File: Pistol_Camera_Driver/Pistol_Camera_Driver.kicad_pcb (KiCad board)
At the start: 2 copper layers, 95.8 x 46.1 mm, 102 parts, among them J1 Screw_Terminal_01x02, J10 Bluetooth, J11 Screw_Terminal_01x02, J12 Screw_Terminal_01x02, J13 I2C, J14 Screw_Terminal_01x02, J15 Screw_Terminal_01x02, J2 Objective, J3 Screw_Terminal_01x02, J4 Screw_Terminal_01x02, J5 Screw_Terminal_01x02, J6 Joystick, J7 Screw_Terminal_01x02, J8 Screw_Terminal_01x02, J9 Screw_Terminal_01x02, K1 IM03, Q1 locked, U1 LM7805_TO220, U2 LM317_TO-263, U3 Raspberri_Pi_Pico, U4 DRV8834PWP, U5 DRV8834PWP

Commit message: V0.2 Seems 2B ready
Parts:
- removed C23: 2u2, Capacitor_SMD:C_0603_1608Metric_Pad1.08x0.95mm_HandSolder
- removed the REF** at (73.6, 74.7)
- removed the REF** at (73.6, 35.6)
- removed the REF** at (27.6, 74.7)
- removed U2: LM317_TO-263, Package_TO_SOT_SMD:TO-263-2
- removed U3: Raspberri_Pi_Pico, Shield_Emergent:Raspberry Pi Pico
- added D2: CDBA3100-HF, Diode_SMD:D_SMA, F.Cu at (96.8, 58.8)
- added J16: Screw_Terminal_01x02, Connector_PinSocket_2.54mm:PinSocket_1x02_P2.54mm_Vertical, F.Cu at (48.3, 62.0)
- added J17: Screw_Terminal_01x02, Connector_PinSocket_2.54mm:PinSocket_1x02_P2.54mm_Vertical, F.Cu at (47.3, 58.4)
- added L5: 22u, Inductor_SMD:L_Sunlord_SWPA4012S, F.Cu at (102.4, 68.1)
- added U10: ~, Vedro:RP2040Zero, F.Cu at (58.1, 47.6)
- C10, C12, C5, C7, C8, R1, R10, R11, R12, R14, R15, R16, R18, R2, R4, R5, R7, R8, R9: moved to F.Cu
- C13, C15, C16, C17, C19, C20, C22: value 2u2 -> 22u
- C2: value 0.33 -> 0.1; moved to F.Cu
- C3: value 0.1 -> 22u; moved to F.Cu
- C4: value 1 -> 470uF; footprint Capacitor_SMD:C_0603_1608Metric_Pad1.08x0.95mm_HandSolder -> Capacitor_THT:CP_Radial_D6.3mm_P2.50mm; moved to F.Cu
- C6: value 1 -> 180uF; footprint Capacitor_SMD:C_0603_1608Metric_Pad1.08x0.95mm_HandSolder -> Capacitor_THT:CP_Radial_D6.3mm_P2.50mm; moved to F.Cu
- J2: moved to B.Cu
- L1, L2, L3, L4: value L -> 4u7; footprint Inductor_SMD:L_12x12mm_H8mm -> Inductor_SMD:L_Chilisin_BMRx00040412
- R3: value 240 -> 4k7; moved to F.Cu
- R6: value 390 -> 4k7; moved to F.Cu
- U1: value LM7805_TO220 -> XL1509-3.3; footprint Package_TO_SOT_THT:TO-220-3_Vertical -> Package_SO:SOIC-8-1EP_3.9x4.9mm_P1.27mm_EP2.95x4.9mm_Mask2.71x3.4mm_ThermalVias
- U4, U5: footprint Shield_Emergent:DRV8834PWP -> Vedro:DRV8834PWP; moved to F.Cu
- locked: renamed from C11; moved to F.Cu
- moved R36 101.4 mm to (79.1, 68.5), turned to 90 degrees
- moved C22 101.4 mm to (73.9, 74.0), turned to 90 degrees
- moved R35 100.9 mm to (80.7, 68.5), turned to 90 degrees
- moved R39 100.6 mm to (77.5, 68.5), turned to 90 degrees
- moved R38 99.4 mm to (76.6, 57.3), turned to 90 degrees
- moved R31 92.6 mm to (78.2, 57.3), turned to 90 degrees
- moved R30 91.5 mm to (79.8, 57.3), turned to 90 degrees
- moved R29 90.4 mm to (81.4, 57.3), turned to 90 degrees
- moved C19 89.6 mm to (73.1, 62.6), turned to 90 degrees
- moved R28 89.4 mm to (83.0, 57.3), turned to 90 degrees
- moved R34 89.3 mm to (82.3, 68.5), turned to 90 degrees
- moved R37 88.9 mm to (85.8, 45.5), turned to 90 degrees
- moved R27 88.5 mm to (84.6, 57.3), turned to 90 degrees
- moved C24 88.5 mm to (84.6, 71.6), turned to 180 degrees
- moved R33 88.2 mm to (83.9, 68.5), turned to 90 degrees
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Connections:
- C14 pad 2: +12V -> +5V
- C15 pad 1: +12V -> +5V
- C16 pad 1: +12V -> +5V
- C18 pad 2: +12V -> +5V
- C19 pad 1: +12V -> +5V
- C2 pad 1: +12V -> +5V
- C20 pad 1: Net-(J9-Pin_1) -> Net-(J12-Pin_1)
- C21 pad 2: +12V -> +5V
- C22 pad 1: +12V -> +5V
- C24 pad 2: +12V -> +5V
- C3 pad 1: +5V -> Net-(J9-Pin_1)
- C4 pad 1: +12V -> +5V
- J10 pad 3: GND -> +3V3
- J10 pad 4: +5V -> GND
- J13 pad 1: SDA -> SCL
- J13 pad 2: SCL -> SDA
- J13 pad 4: +5V -> +3V3
- J3 pad 1: +12V -> +5V
- J4 pad 1: +12V -> +5V
- R17 pad 1: Solenoid_DIR -> Solenoid_ON
- R19 pad 1: Solenoid_ON -> Solenoid_DIR
- R3 pad 1: +3.3VP -> +3V3
- R3 pad 2: Net-(U2-ADJ) -> SCL
- R6 pad 1: Net-(U2-ADJ) -> +3V3
- R6 pad 2: GND -> SDA
- U1 pad 1: +12V -> +5V
- U1 pad 2: GND -> Net-(U1-OUT)
- U1 pad 3: +5V -> +3.3VP
- U6 pad 3: +12V -> +5V
- U6 pad 4: PWM_UV -> PWM_WHITE
- U6 pad 8: +12V -> +5V
- U7 pad 3: +12V -> +5V
- U7 pad 4: PWM_WHITE -> PWM_RED
- U7 pad 8: +12V -> +5V
- U8 pad 3: +12V -> +5V
- U8 pad 4: PWM_RED -> PWM_UV
- U8 pad 8: +12V -> +5V
- U9 pad 3: +12V -> +5V
- U9 pad 8: +12V -> +5V
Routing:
- net +12V: track 115.9 -> 0.00 mm
- net +3V3: track 174.5 -> 116.5 mm, vias 5 -> 1
- net Solenoid_ON: track 3.29 -> 39.3 mm, vias 0 -> 2
- net MOTORS_nSLEEP: track 104.2 -> 71.9 mm, vias 3 -> 2
- net Solenoid_DIR: track 4.58 -> 36.0 mm, vias 0 -> 2
- net +3.3VP: track 114.8 -> 94.6 mm, vias 1 -> 0
- net PWM_WHITE: track 38.7 -> 23.0 mm
- net K3: track 9.70 -> 24.9 mm, vias 0 -> 2
- net K4: track 5.67 -> 20.2 mm, vias 0 -> 2
- net GND: track 30.1 -> 17.7 mm, vias 307 -> 213
- net (no net): track 11.9 -> 0.00 mm, vias 1 -> 0
- net nFLT2: track 56.2 -> 67.1 mm
- net STEP1: track 61.9 -> 51.2 mm
- net DIR1: track 60.1 -> 49.3 mm
- net nEN2: track 54.2 -> 43.8 mm
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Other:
- board size 95.8 x 46.1 mm -> 83.3 x 46.1 mm

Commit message: V0.3 Ordered
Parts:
- added REF**: MountingHole_3.2mm_M3, MountingHole:MountingHole_3.2mm_M3, F.Cu at (40.6, 74.7)
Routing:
- net GND: vias 213 -> 215
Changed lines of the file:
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@@
     (property "ki_keywords" "R res resistor")
     (attr smd)
-    (fp_text reference "R10" (at 0.25 2.25) (layer "F.SilkS")
+    (fp_text reference "R10" (at -3.6 0.65) (layer "F.SilkS")
         (effects (font (size 1 1) (thickness 0.15)))
     )
@@
     )
   )
+  (footprint "MountingHole:MountingHole_3.2mm_M3" locked (layer "F.Cu")
+    (at 40.645 74.65)
+    (descr "Mounting Hole 3.2mm, no annular, M3")
+    (tags "mounting hole 3.2mm no annular m3")
+    (attr exclude_from_pos_files exclude_from_bom)
+    (fp_text reference "REF**" (at 0 -4.2) (layer "F.SilkS") hide
+        (effects (font (size 1 1) (thickness 0.15)))
+    )
+    (fp_text value "MountingHole_3.2mm_M3" (at 0 4.2) (layer "F.Fab") hide
+        (effects (font (size 1 1) (thickness 0.15)))
+    )
+    (fp_text user "${REFERENCE}" (at 0 0) (layer "F.Fab") hide
+        (effects (font (size 1 1) (thickness 0.15)))
+    )
+    (fp_circle (center 0 0) (end 3.2 0)
+      (stroke (width 0.15) (type solid)) (fill none) (layer "Cmts.User"))
+    (fp_circle (center 0 0) (end 3.45 0)
+      (stroke (width 0.05) (type solid)) (fill none) (layer "F.CrtYd"))
+    (pad "" np_thru_hole circle locked (at 0 0) (size 3.2 3.2) (drill 3.2) (layers "F&B.Cu" "*.Mask"))
+  )
   (footprint "Capacitor_SMD:C_0603_1608Metric_Pad1.08x0.95mm_HandSolder" (layer "F.Cu")
     (at 112.65 41.85 180)
@@
     (property "ki_keywords" "diode Schottky")
     (attr smd)
-    (fp_text reference "D2" (at 0 -2.5 90) (layer "F.SilkS")
+    (fp_text reference "D2" (at -0.7 -2.5 90) (layer "F.SilkS")
         (effects (font (size 1 1) (thickness 0.15)))
     )
@@
         (effects (font (size 1 1) (thickness 0.15)) (justify mirror))
     )
-    (fp_text value "Objective" (at 2.875 -2.75) (layer "B.SilkS")
-        (effects (font (size 1 1) (thickness 0.15)) (justify mirror))
+    (fp_text value "Objective" (at -1.325 -2.9 180) (layer "F.SilkS")
+        (effects (font (size 1 1) (thickness 0.15)))
     )
     (fp_text user "${REFERENCE}" (at -2.525 -4.95) (layer "B.Fab")
@@
   (via (at 70.6 35.2) (size 0.9) (drill 0.4) (layers "F.Cu" "B.Cu") (free) (net 2))
   (via (at 75.25 49) (size 0.9) (drill 0.4) (layers "F.Cu" "B.Cu") (free) (net 2))
-  (via (at 84.628637 62.668266) (size 0.9) (drill 0.4) (layers "F.Cu" "B.Cu") (free) (net 2))
+  (via (at 85.65 61.9) (size 0.9) (drill 0.4) (layers "F.Cu" "B.Cu") (free) (net 2))
   (via (at 91 32.1) (size 0.9) (drill 0.4) (layers "F.Cu" "B.Cu") (free) (net 2))
   (via (at 38.9 40.5) (size 0.9) (drill 0.4) (layers "F.Cu" "B.Cu") (free) (net 2))
@@
   (via (at 118.55 63.95) (size 0.9) (drill 0.4) (layers "F.Cu" "B.Cu") (free) (net 2))
   (via (at 74.95 56.25) (size 0.9) (drill 0.4) (layers "F.Cu" "B.Cu") (free) (net 2))
+  (via (at 84.05 62.3) (size 0.9) (drill 0.4) (layers "F.Cu" "B.Cu") (free) (net 2))
   (via (at 38.65 46.75) (size 0.9) (drill 0.4) (layers "F.Cu" "B.Cu") (free) (net 2))
   (via (at 68.4 46.1) (size 0.9) (drill 0.4) (layers "F.Cu" "B.Cu") (free) (net 2))
@@
   (via (at 61.781858 41.884493) (size 0.9) (drill 0.4) (layers "F.Cu" "B.Cu") (free) (net 2))
   (via (at 99.5 37.35) (size 0.9) (drill 0.4) (layers "F.Cu" "B.Cu") (free) (net 2))
+  (via (at 82.35 62.25) (size 0.9) (drill 0.4) (layers "F.Cu" "B.Cu") (free) (net 2))
   (via (at 89.8 43.4) (size 0.9) (drill 0.4) (layers "F.Cu" "B.Cu") (free) (net 2))
   (via (at 116.9 64.95) (size 0.9) (drill 0.4) (layers "F.Cu" "B.Cu") (free) (net 2))

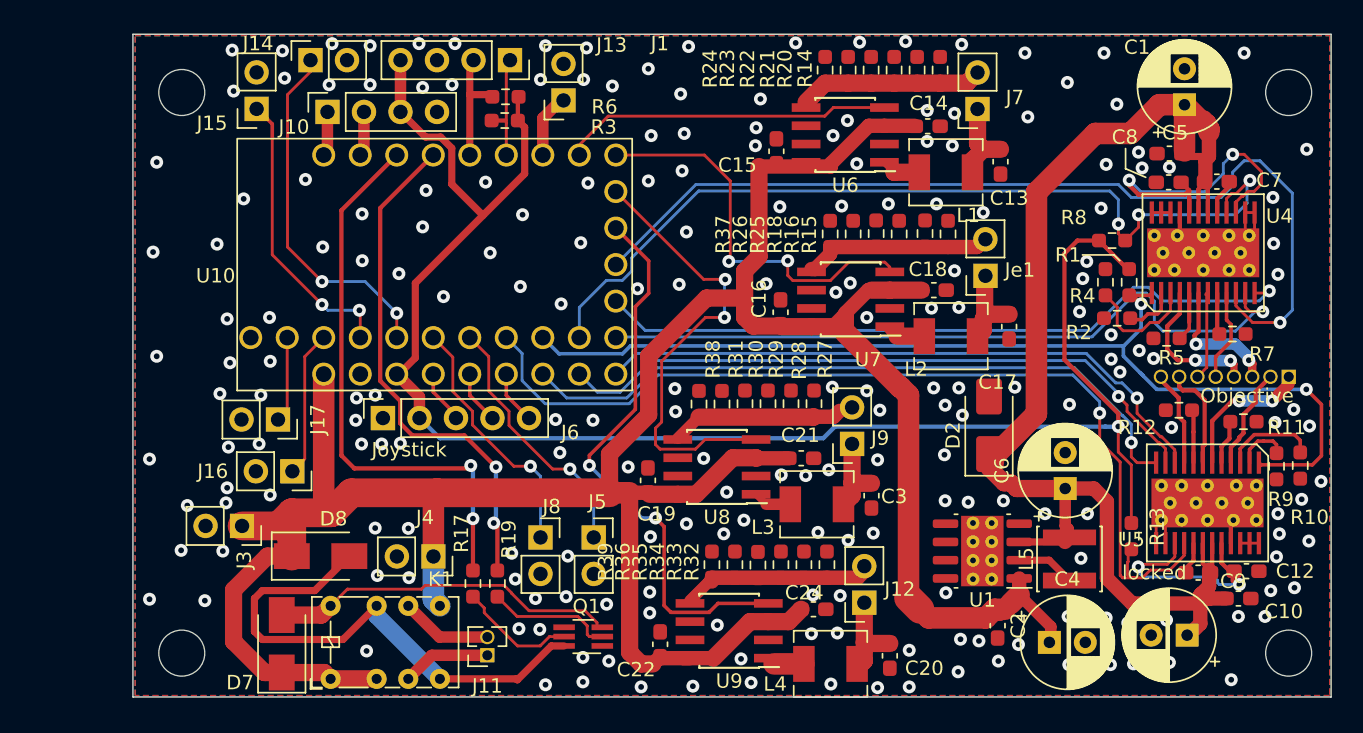
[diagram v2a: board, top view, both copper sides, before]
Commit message: v0.4 5 V DC/CD was added, Relay was changed to the H-bridge
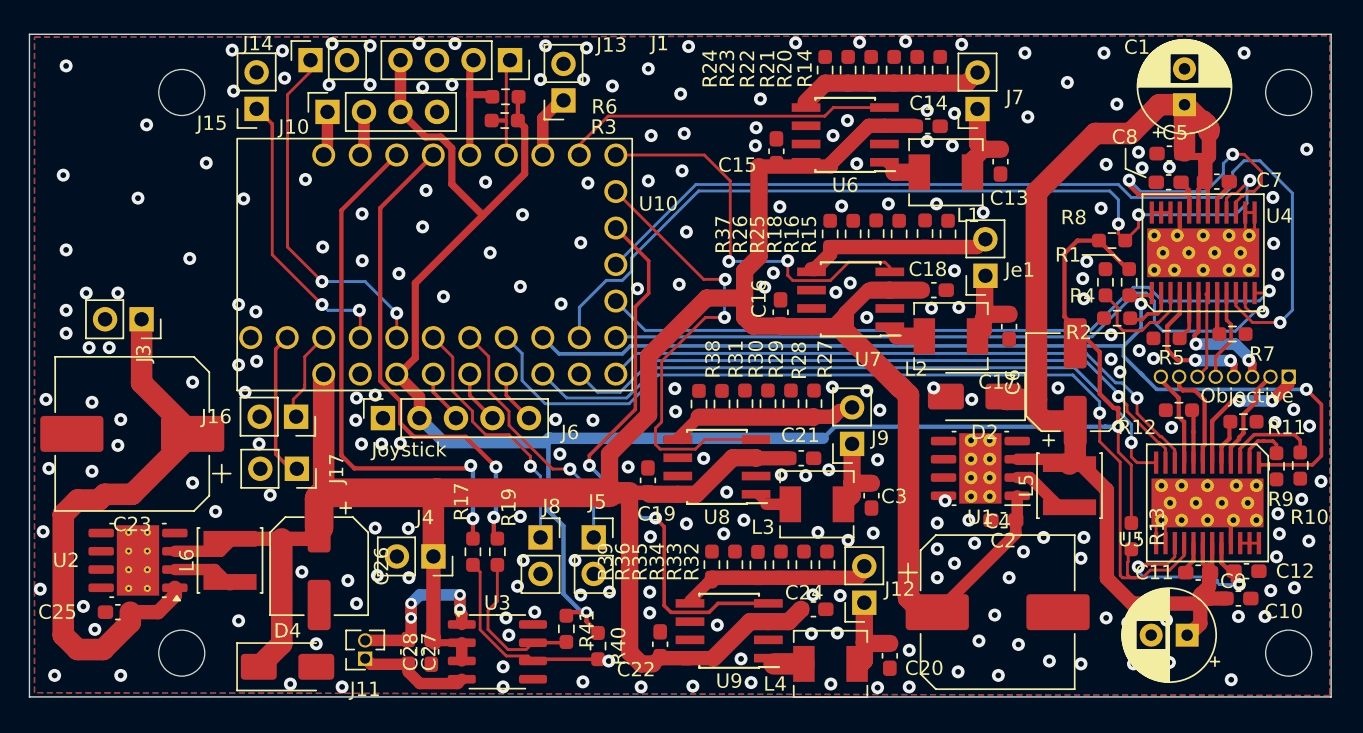
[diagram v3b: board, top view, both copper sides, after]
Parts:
- removed D7, D8: CDBA3100-HF, Diode_SMD:D_SMA
- removed K1: IM03, Relay_THT:Relay_DPDT_AXICOM_IMSeries_Pitch5.08mm
- removed Q1: locked, Package_TO_SOT_SMD:SOT-363_SC-70-6_Handsoldering
- added C23: 470uF, Capacitor_SMD:CP_Elec_10x10.5, F.Cu at (37.2, 59.4)
- added C25: 0.1, Capacitor_SMD:C_0603_1608Metric_Pad1.08x0.95mm_HandSolder, F.Cu at (36.2, 71.8)
- added C26: 180uF, Capacitor_SMD:CP_Elec_6.3x7.7, F.Cu at (50.2, 68.6)
- added C27: 0.1, Capacitor_SMD:C_0603_1608Metric_Pad1.08x0.95mm_HandSolder, F.Cu at (56.4, 74.6)
- added C28: 0.1, Capacitor_SMD:C_0603_1608Metric_Pad1.08x0.95mm_HandSolder, F.Cu at (58.0, 74.6)
- added D4: CDBA3100-HF, Diode_SMD:D_SMA, F.Cu at (48.0, 75.6)
- added L6: 22u, Inductor_SMD:L_Sunlord_SWPA4012S, F.Cu at (44.0, 68.2)
- added R40: 10k, Resistor_SMD:R_0603_1608Metric_Pad0.98x0.95mm_HandSolder, F.Cu at (69.6, 74.2)
- added R41: 10k, Resistor_SMD:R_0603_1608Metric_Pad0.98x0.95mm_HandSolder, F.Cu at (67.4, 73.0)
- added U2: XL1509-5.0, Package_SO:SOIC-8-1EP_3.9x4.9mm_P1.27mm_EP2.95x4.9mm_Mask2.71x3.4mm_ThermalVias, F.Cu at (37.6, 68.2)
- added U3: ~, Package_SO:SOIC-8_3.9x4.9mm_P1.27mm, F.Cu at (62.6, 74.6)
- C4: footprint Capacitor_THT:CP_Radial_D6.3mm_P2.50mm -> Capacitor_SMD:CP_Elec_10x10.5
- C6: footprint Capacitor_THT:CP_Radial_D6.3mm_P2.50mm -> Capacitor_SMD:CP_Elec_6.3x7.7
- moved J3 16.0 mm to (37.9, 51.4)
- moved J11 8.50 mm to (53.4, 75.0)
- moved C6 7.43 mm to (102.8, 55.8)
- moved C2 7.35 mm to (97.8, 65.4), turned to 180 degrees
- moved U1 5.75 mm to (96.2, 61.8)
- moved L5 5.10 mm to (102.4, 63.0)
- moved C4 4.17 mm to (97.4, 71.8)
- moved J16 3.81 mm to (48.6, 58.2)
- moved J17 3.67 mm to (48.6, 61.8)
- moved D2 2.24 mm to (95.8, 56.8), turned to 180 degrees
- moved R17 2.21 mm to (60.9, 67.6)
- moved R19 2.21 mm to (62.6, 67.6)
- renumbered locked to C11
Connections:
- J3 pad 1: +5V -> VPP
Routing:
- net VPP: track 0.00 -> 39.9 mm
- net Net-(D8-A): track 36.4 -> 0.00 mm
- net Net-(D7-A): track 24.2 -> 0.00 mm
- net +3V3: track 116.5 -> 133.6 mm, vias 1 -> 2
- net Net-(J11-Pin_2): track 6.41 -> 13.4 mm, vias 0 -> 4
- net +3.3VP: track 94.6 -> 89.5 mm
- net Net-(U3-IA): track 8.80 -> 13.9 mm
- net +5V: track 197.9 -> 193.2 mm
- net Net-(U2-OUT): track 0.00 -> 4.28 mm
- net K6: track 5.97 -> 10.2 mm
- net K5: track 10.2 -> 6.58 mm
- net Net-(U3-IB): track 8.43 -> 11.0 mm
- net Solenoid_ON: track 39.3 -> 37.1 mm
- net Solenoid_DIR: track 36.0 -> 34.2 mm
- net Net-(J11-Pin_1): track 6.19 -> 7.88 mm
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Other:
- board size 83.3 x 46.1 mm -> 90.5 x 46.1 mm
